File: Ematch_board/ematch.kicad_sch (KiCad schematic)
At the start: 56 parts, among them J1 Conn_01x02_Male, J2 Conn_01x02_Male, J3 Conn_01x02_Male, J4 Conn_01x02_Male, J5 Conn_01x02_Male, J6 Conn_01x02_Male, Q51 PMV20ENR, Q52 PMV20ENR, Q53 PMV20ENR, Q54 PMV20ENR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

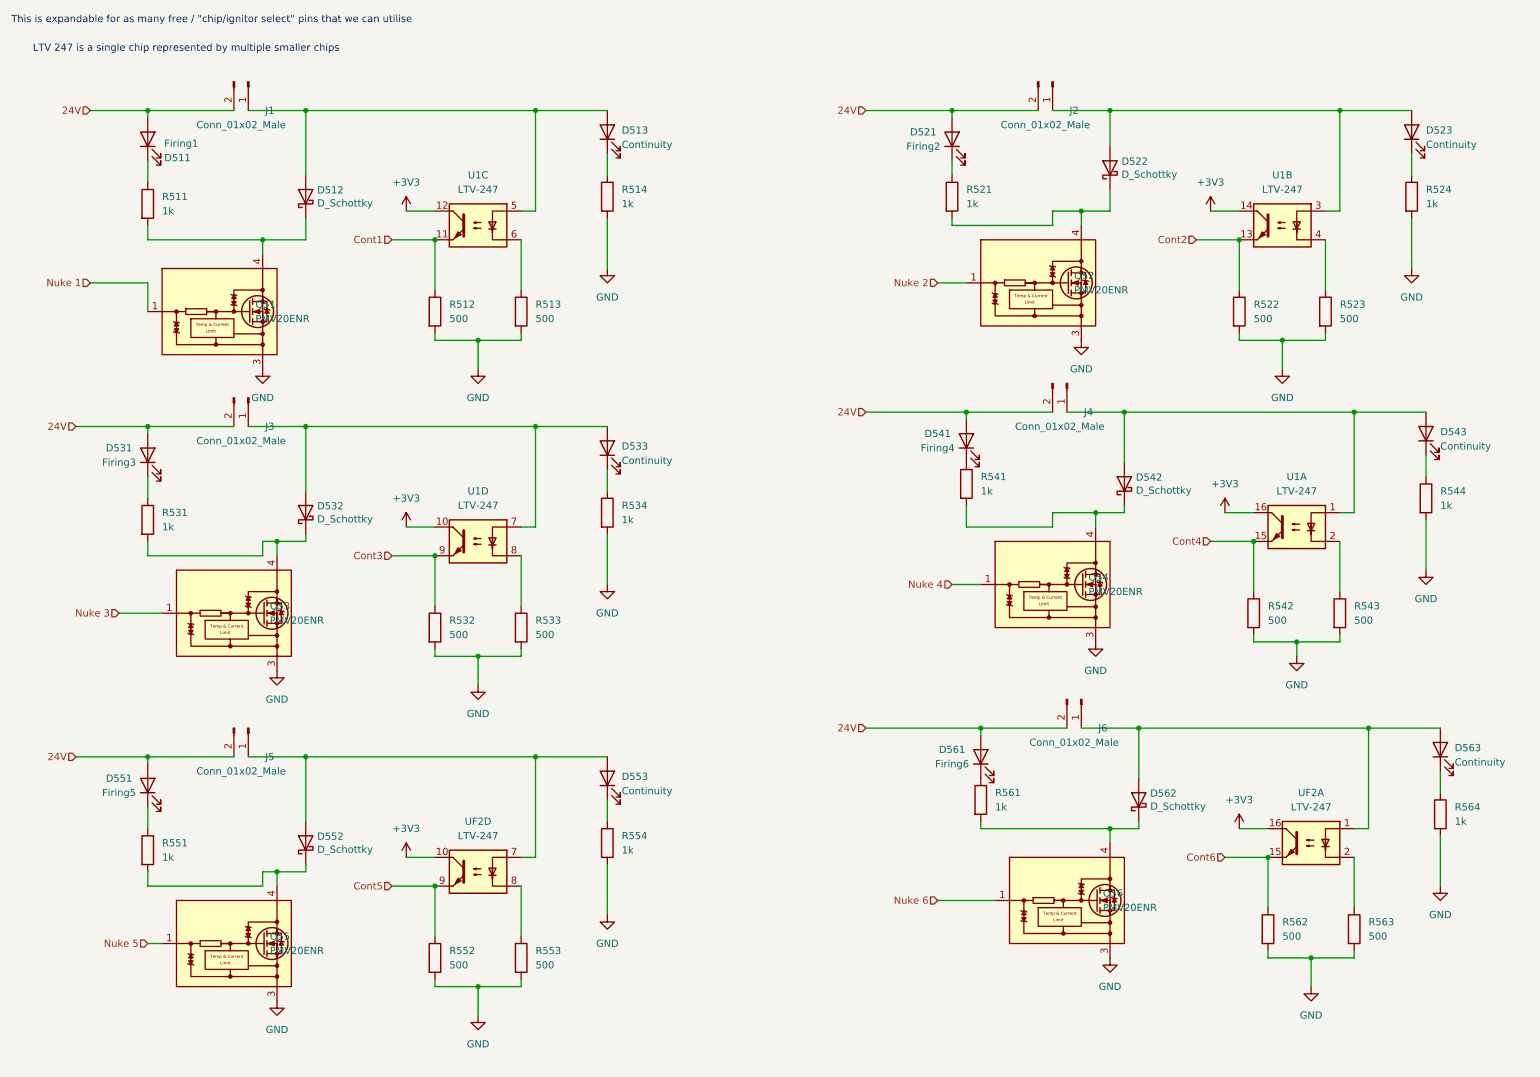
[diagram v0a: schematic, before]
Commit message: changed schottky diode FP and rearranged mosfets + screw terminals
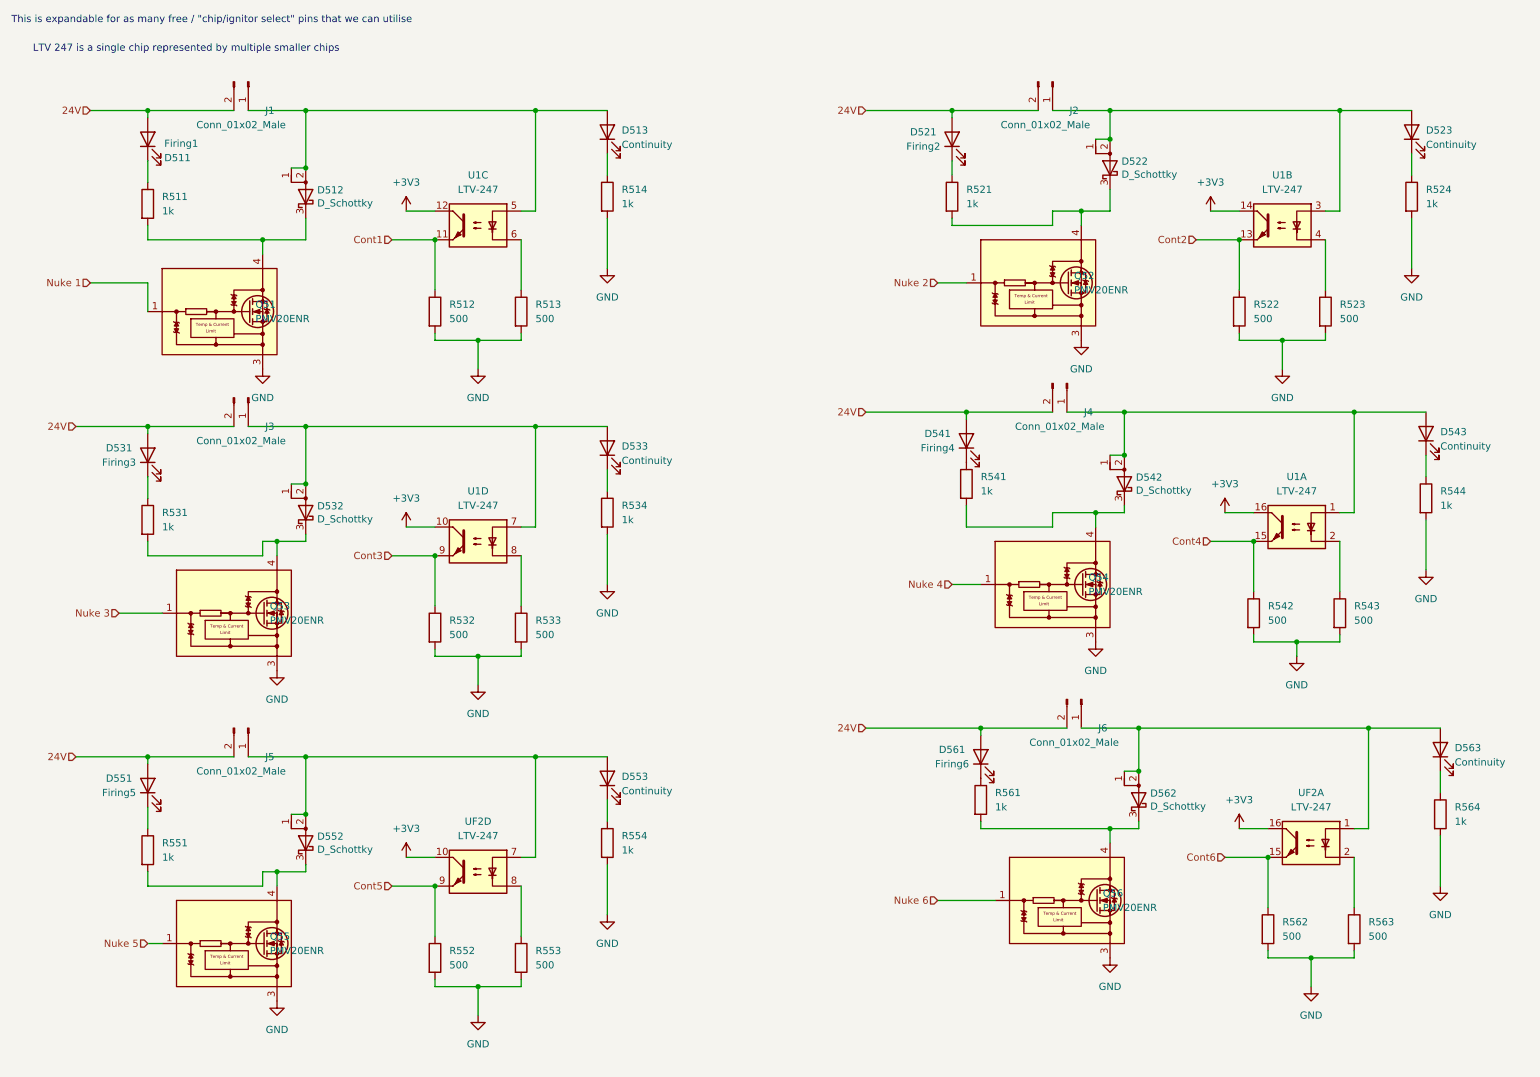
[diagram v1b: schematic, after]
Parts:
- D512, D522, D532, D542, D552, D562: footprint Diode_SMD:D_SOD-128 -> Package_TO_SOT_SMD:TO-277B; symbol Device:D_Schottky -> Device:D_Schottky_AAK
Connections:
- net at Q51.2 (D), Q51.4 (D), R511.2: now also D512.3 (K); no longer D512.1 (K)
- net at D512.2 (A), D513.2 (A), J1.1 (Pin_1)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: now also D512.1 (A)
- net at D522.2 (A), D523.2 (A), J2.1 (Pin_1)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: now also D522.1 (A)
- net at D542.2 (A), D543.2 (A), J4.1 (Pin_1)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: now also D542.1 (A)
- net at D552.2 (A), D553.2 (A), J5.1 (Pin_1)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: now also D552.1 (A)
- net at D532.2 (A), D533.2 (A), J3.1 (Pin_1)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: now also D532.1 (A)
- net at Q52.2 (D), Q52.4 (D), R521.2: now also D522.3 (K); no longer D522.1 (K)
- net at Q55.2 (D), Q55.4 (D), R551.2: now also D552.3 (K); no longer D552.1 (K)
- net at D562.2 (A), D563.2 (A), J6.1 (Pin_1)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: now also D562.1 (A)
- net at Q53.2 (D), Q53.4 (D), R531.2: now also D532.3 (K); no longer D532.1 (K)
- net at Q56.2 (D), Q56.4 (D), R561.2: now also D562.3 (K); no longer D562.1 (K)
- net at Q54.2 (D), Q54.4 (D), R541.2: now also D542.3 (K); no longer D542.1 (K)

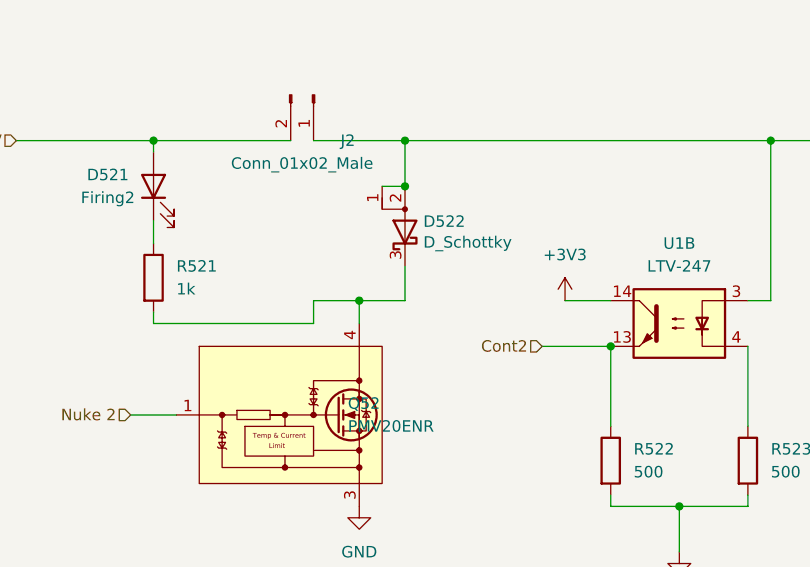
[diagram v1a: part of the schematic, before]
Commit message: completed layout for screw terminals, moved some LEDs
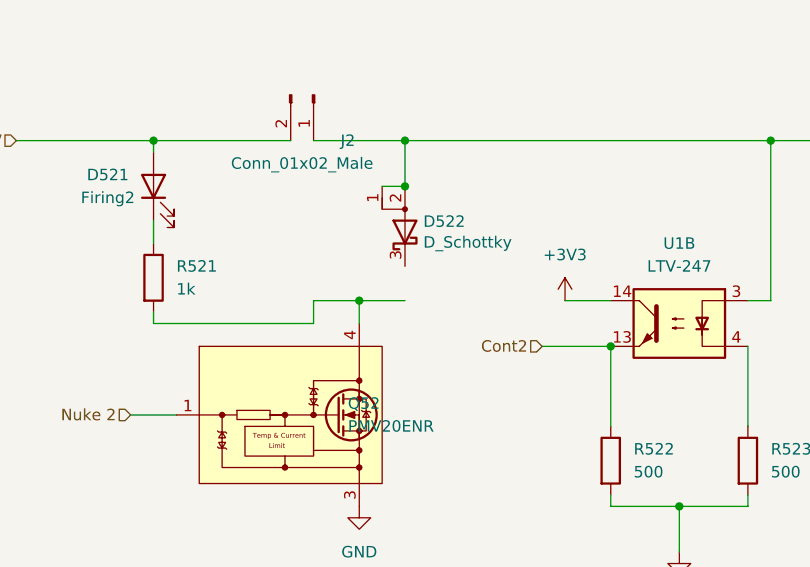
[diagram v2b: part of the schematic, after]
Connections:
- net at Q52.2 (D), Q52.4 (D), R521.2: no longer D522.3 (K)
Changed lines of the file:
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@@
-    (stroke (width 0) (type default) (color 0 0 0 0))
-  )
-  (wire (pts (xy 208.28 44.45) (xy 208.28 48.26))
     (stroke (width 0) (type default) (color 0 0 0 0))
   )

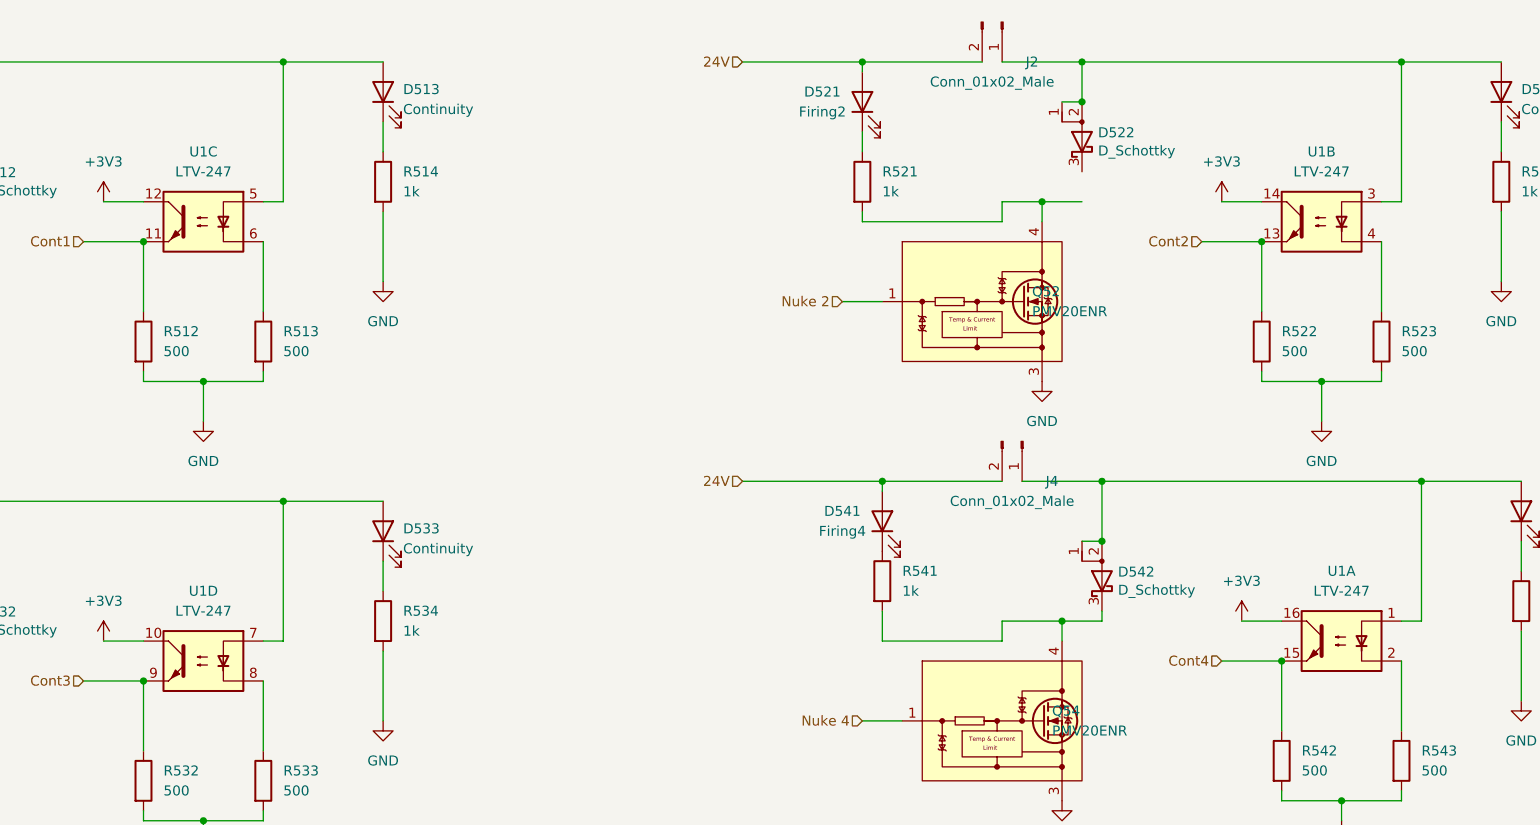
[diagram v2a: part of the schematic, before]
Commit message: completed routing, changed antenna for U.FL connector
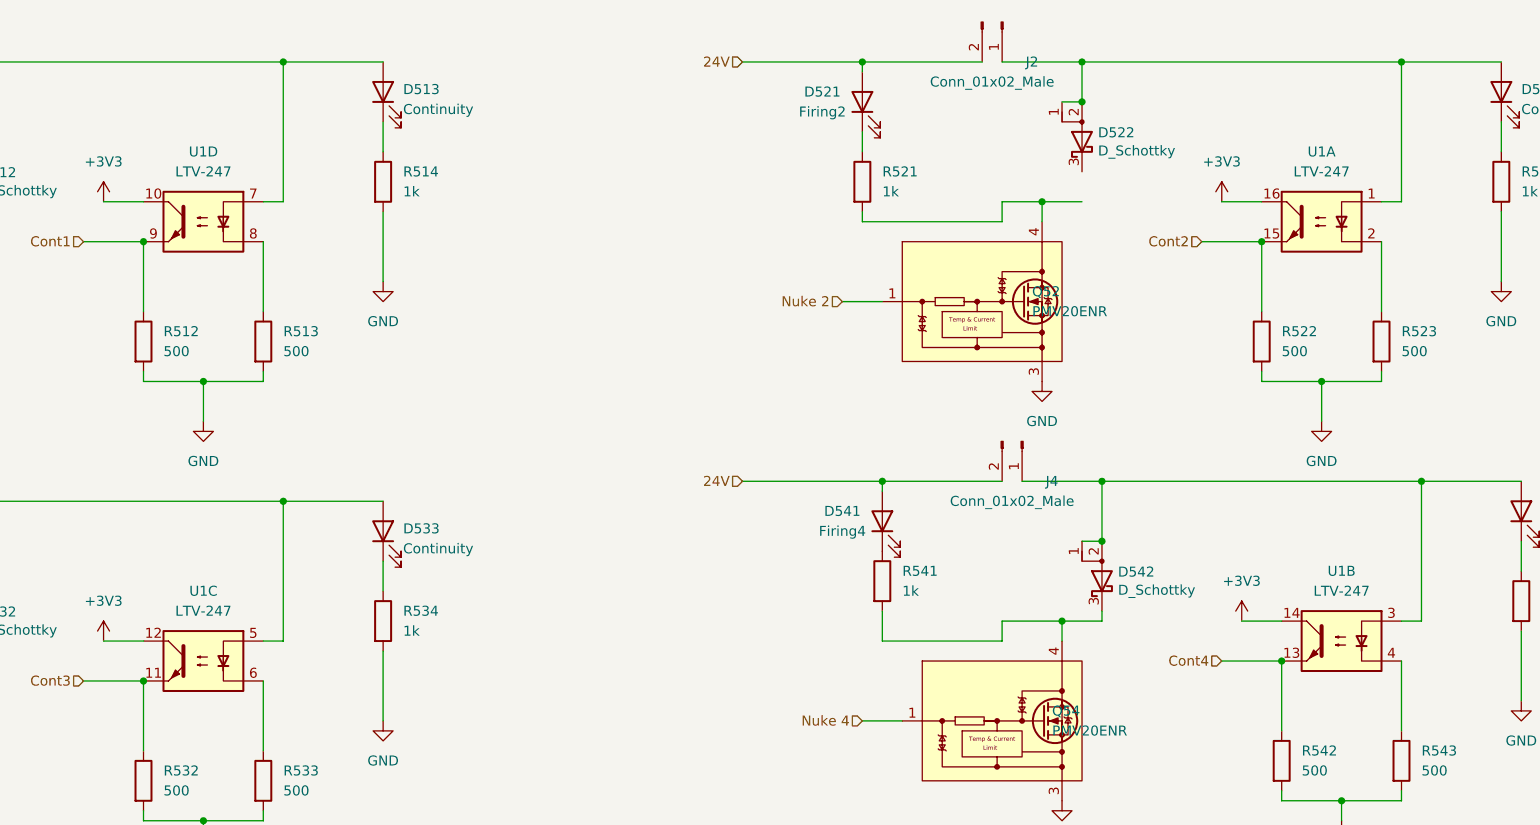
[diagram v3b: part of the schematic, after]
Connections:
- net +3V3: now also U1.14, U1.16; no longer U1.14, U1.16
- net Cont1: now also U1.9; no longer U1.11
- net Cont2: now also U1.15; no longer U1.13
- net Cont3: now also U1.11; no longer U1.9
- net Cont4: now also U1.13; no longer U1.15
- net at D512.1 (A), D512.2 (A), D513.2 (A)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: now also U1.7; no longer U1.5
- net at D522.1 (A), D522.2 (A), D523.2 (A)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: now also U1.1; no longer U1.3
- net at R523.1: now also U1.2; no longer U1.4
- net at D542.1 (A), D542.2 (A), D543.2 (A)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: now also U1.3; no longer U1.1
- net at D532.1 (A), D532.2 (A), D533.2 (A)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: now also U1.5; no longer U1.7
- net at R533.1: now also U1.6; no longer U1.8
- net at R513.1: now also U1.8; no longer U1.6
- net at R543.1: now also U1.4; no longer U1.2

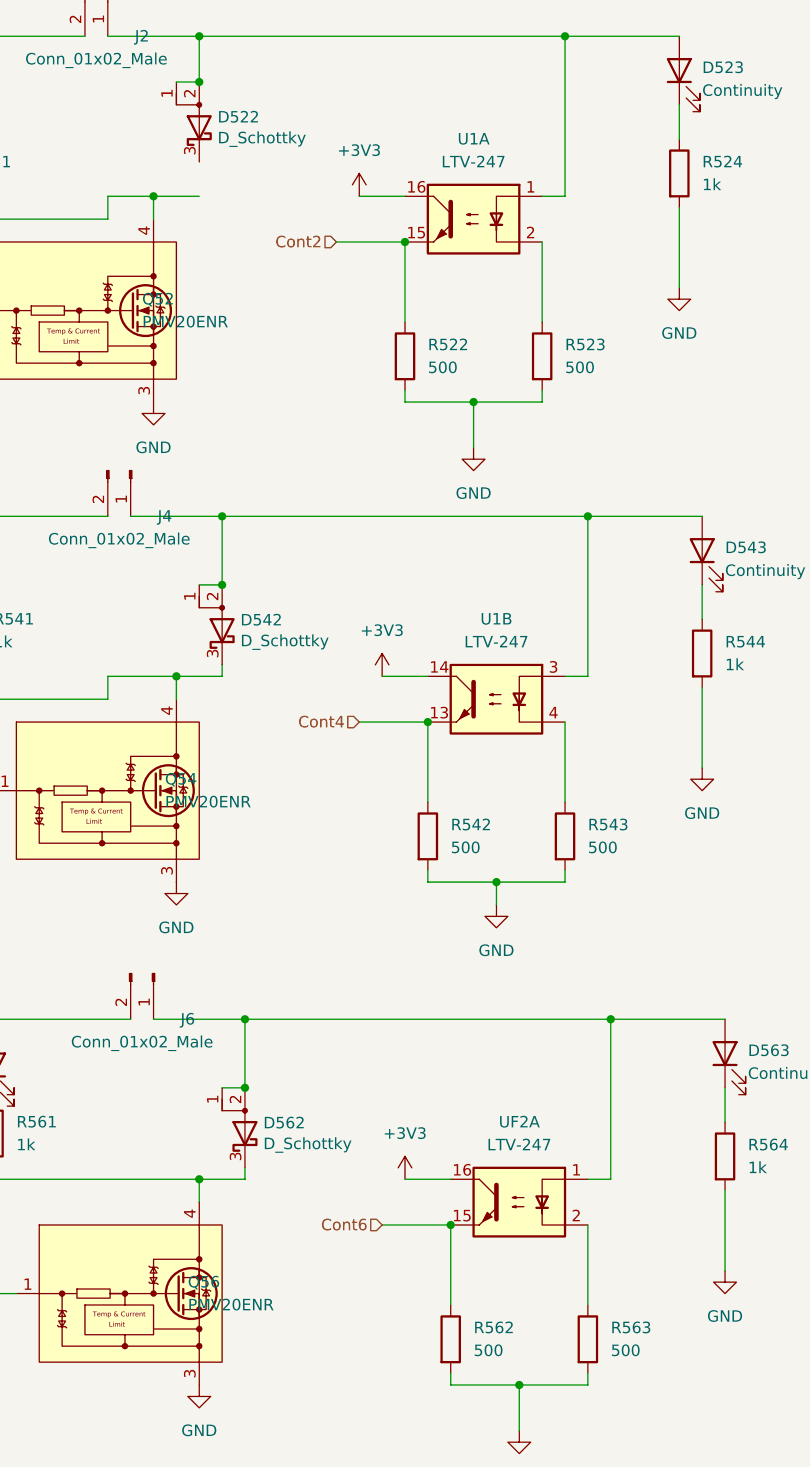
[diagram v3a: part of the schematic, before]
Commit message: created GND planes and fixed zone priority to prevent shorting nets
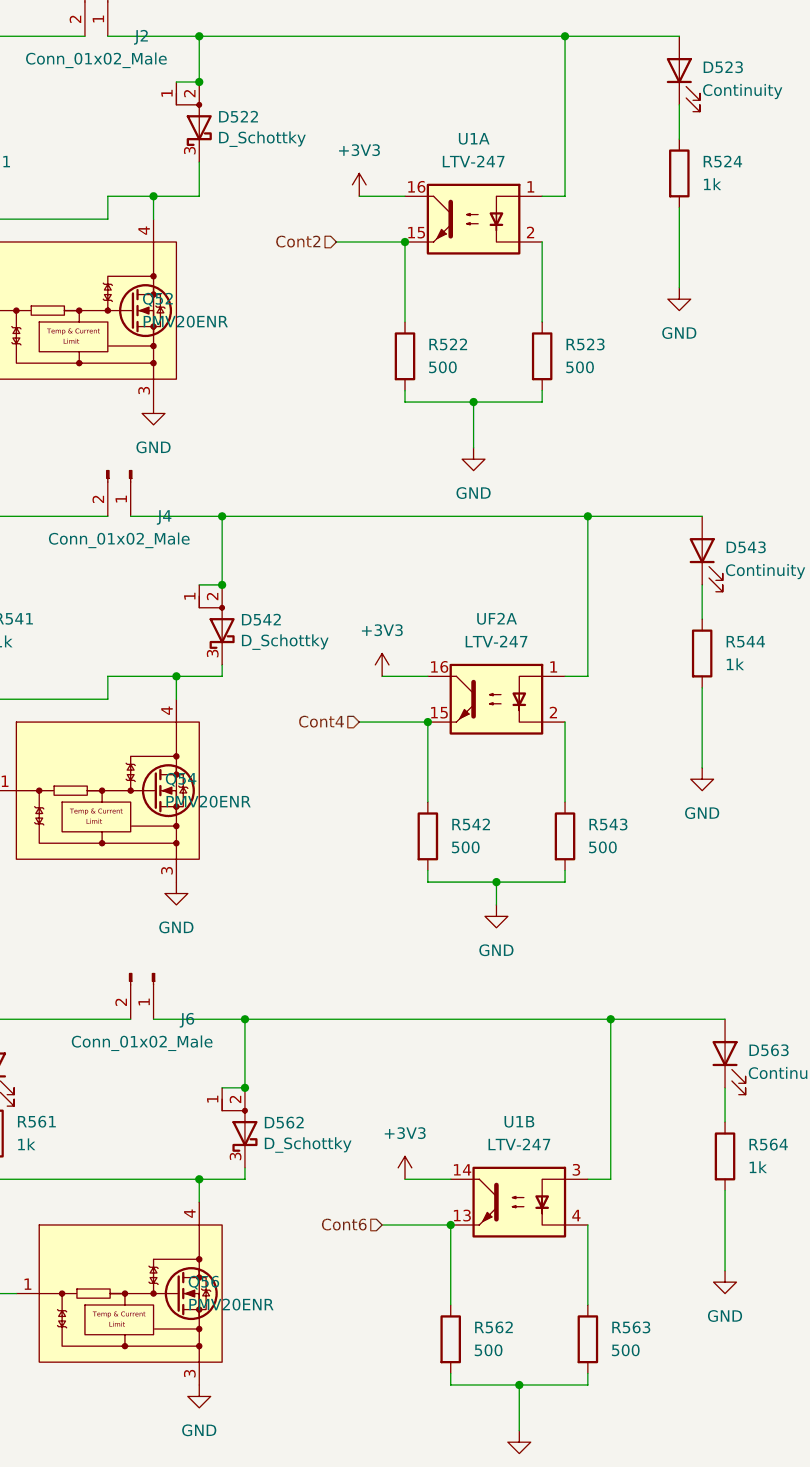
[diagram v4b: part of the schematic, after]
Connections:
- net Cont4: now also UF2.15; no longer U1.13
- net Cont6: now also U1.13; no longer UF2.15
- net at D542.1 (A), D542.2 (A), D543.2 (A)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: now also UF2.1; no longer U1.3
- net at D522.3 (K): now also Q52.2 (D), Q52.4 (D), R521.2
- net at D562.1 (A), D562.2 (A), D563.2 (A)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: now also U1.3; no longer UF2.1
- net at R563.1: now also U1.4; no longer UF2.2
- net at R543.1: now also UF2.2; no longer U1.4
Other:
- moved on the sheet: U1B, UF2A
